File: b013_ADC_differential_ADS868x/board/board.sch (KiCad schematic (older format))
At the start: 8 parts, among them J1 002_SPI_2x5, J2 007_ADC_2x5, U1 ADS8689RUM

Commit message: added part info for silicon parts
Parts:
- U1: MPN (none) -> ADS8689RUM
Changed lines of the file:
@@
 F 2 "Package_DFN_QFN:QFN-16-1EP_4x4mm_P0.65mm_EP2.7x2.7mm" H 6425 2850 50  0001 C CNN
 F 3 "http://www.ti.com/lit/ds/symlink/ads8681.pdf" H 6475 4000 50  0001 C CNN
+F 4 "ADS8689RUM" H 6425 3750 50  0001 C CNN "MPN"
 	1    6425 3750
 	-1   0    0    -1

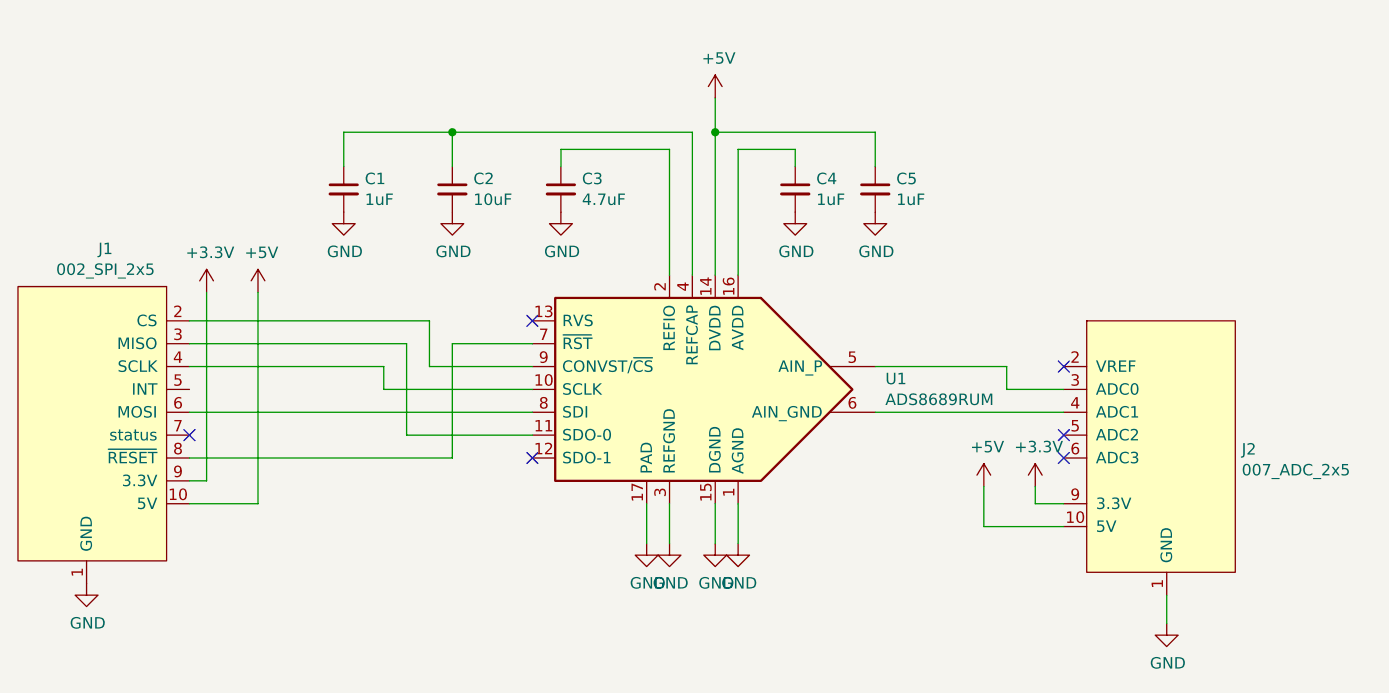
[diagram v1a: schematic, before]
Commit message: changed b013 to use 3.3v as IO voltage and fixed supply voltage bug
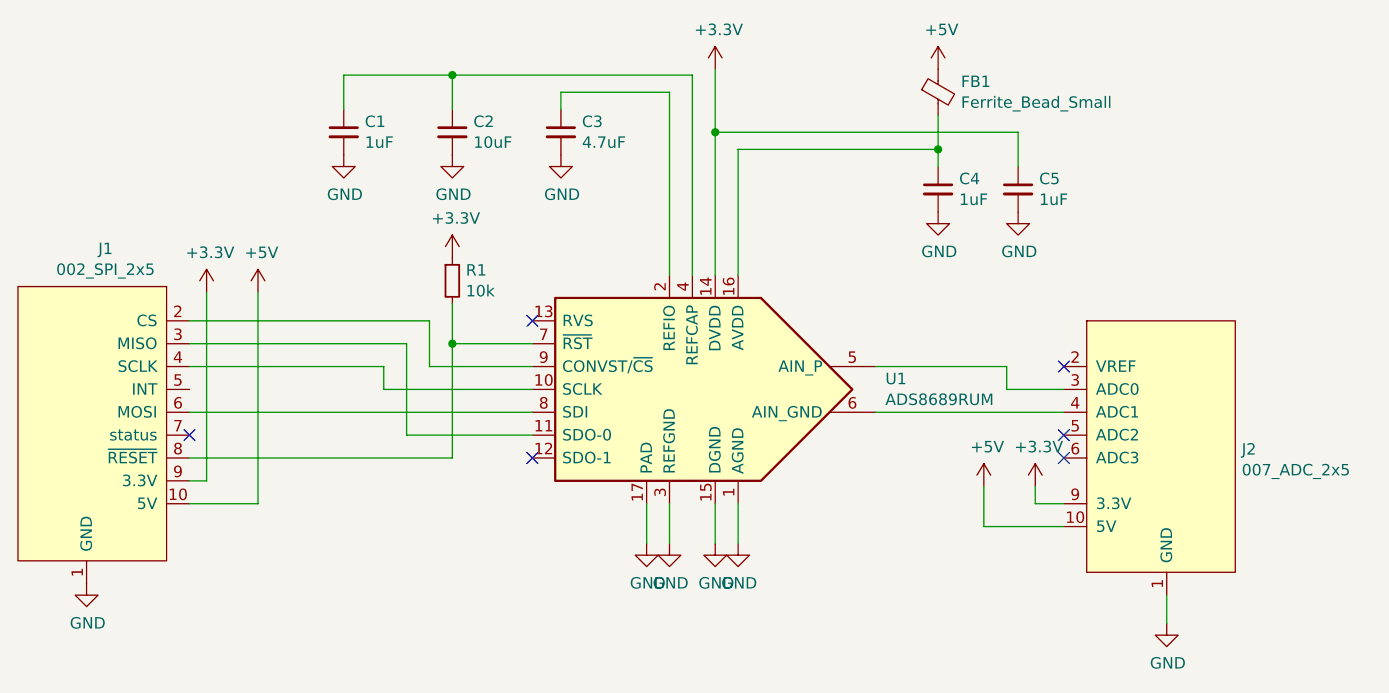
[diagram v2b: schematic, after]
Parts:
- added FB1: Ferrite_Bead_Small, Inductor_SMD:L_0603_1608Metric, symbol Device:Ferrite_Bead_Small
- added R1: 10k, Resistor_SMD:R_0603_1608Metric, symbol Device:R_Small
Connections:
- net +3V3: now also C5.1, U1.14 (DVDD), R1.1
- net +5V: now also FB1.1; no longer C5.1, U1.14 (DVDD)
- net at J1.8 (~RESET), U1.7 (~RST): now also R1.2
- net at C4.1, U1.16 (AVDD): now also FB1.2
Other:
- moved on the sheet: C1, C2, C3, C4, C5
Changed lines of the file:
@@
 L Device:C_Small C2
 U 1 1 60335A70
-P 5275 2875
-F 0 "C2" H 5367 2921 50  0000 L CNN
-F 1 "10uF" H 5367 2830 50  0000 L CNN
-F 2 "Capacitor_SMD:C_0603_1608Metric" H 5275 2875 50  0001 C CNN
-F 3 "~" H 5275 2875 50  0001 C CNN
-	1    5275 2875
+P 5275 2625
+F 0 "C2" H 5367 2671 50  0000 L CNN
+F 1 "10uF" H 5367 2580 50  0000 L CNN
+F 2 "Capacitor_SMD:C_0603_1608Metric" H 5275 2625 50  0001 C CNN
+F 3 "~" H 5275 2625 50  0001 C CNN
+	1    5275 2625
 	1    0    0    -1
 $EndComp
@@
 L Device:C_Small C1
 U 1 1 60336AFF
-P 4800 2875
-F 0 "C1" H 4892 2921 50  0000 L CNN
-F 1 "1uF" H 4892 2830 50  0000 L CNN
-F 2 "Capacitor_SMD:C_0603_1608Metric" H 4800 2875 50  0001 C CNN
-F 3 "~" H 4800 2875 50  0001 C CNN
-	1    4800 2875
-	1    0    0    -1
-$EndComp
-Wire Wire Line
-	4800 2775 4800 2625
-Wire Wire Line
-	4800 2625 5275 2625
-Wire Wire Line
-	5275 2625 5275 2775
-Wire Wire Line
-	6325 2625 6325 3250
-Connection ~ 5275 2625
-Wire Wire Line
-	5275 2625 6325 2625
+P 4800 2625
+F 0 "C1" H 4892 2671 50  0000 L CNN
+F 1 "1uF" H 4892 2580 50  0000 L CNN
+F 2 "Capacitor_SMD:C_0603_1608Metric" H 4800 2625 50  0001 C CNN
+F 3 "~" H 4800 2625 50  0001 C CNN
+	1    4800 2625
+	1    0    0    -1
+$EndComp
+Wire Wire Line
+	4800 2525 4800 2375
+Wire Wire Line
+	4800 2375 5275 2375
+Wire Wire Line
+	5275 2375 5275 2525
+Connection ~ 5275 2375
+Wire Wire Line
+	5275 2375 6325 2375
 $Comp
 L Device:C_Small C3
 U 1 1 60338ADE
-P 5750 2875
-F 0 "C3" H 5842 2921 50  0000 L CNN
-F 1 "4.7uF" H 5842 2830 50  0000 L CNN
-F 2 "Capacitor_SMD:C_0603_1608Metric" H 5750 2875 50  0001 C CNN
-F 3 "~" H 5750 2875 50  0001 C CNN
-	1    5750 2875
-	1    0    0    -1
-$EndComp
-Wire Wire Line
-	5750 2775 5750 2700
-Wire Wire Line
-	5750 2700 6225 2700
-Wire Wire Line
-	6225 2700 6225 3250
+P 5750 2625
+F 0 "C3" H 5842 2671 50  0000 L CNN
+F 1 "4.7uF" H 5842 2580 50  0000 L CNN
+F 2 "Capacitor_SMD:C_0603_1608Metric" H 5750 2625 50  0001 C CNN
+F 3 "~" H 5750 2625 50  0001 C CNN
+	1    5750 2625
+	1    0    0    -1
+$EndComp
+Wire Wire Line
+	5750 2525 5750 2450
+Wire Wire Line
+	5750 2450 6225 2450
 $Comp
 L put_on_edge:002_SPI_2x5 J1
@@
 L power:+5V #PWR0102
 U 1 1 603458CA
-P 6425 2475
-F 0 "#PWR0102" H 6425 2325 50  0001 C CNN
-F 1 "+5V" H 6440 2648 50  0000 C CNN
-F 2 "" H 6425 2475 50  0001 C CNN
-F 3 "" H 6425 2475 50  0001 C CNN
-	1    6425 2475
-	1    0    0    -1
-$EndComp
-Wire Wire Line
-	6425 2475 6425 2625
+P 7400 2350
+F 0 "#PWR0102" H 7400 2200 50  0001 C CNN
+F 1 "+5V" H 7415 2523 50  0000 C CNN
+F 2 "" H 7400 2350 50  0001 C CNN
+F 3 "" H 7400 2350 50  0001 C CNN
+	1    7400 2350
+	1    0    0    -1
+$EndComp
+Wire Wire Line
+	7400 2550 7400 2700
 $Comp
 L power:GND #PWR0103
@@
 L power:GND #PWR0107
 U 1 1 603473AA
-P 5750 2975
-F 0 "#PWR0107" H 5750 2725 50  0001 C CNN
-F 1 "GND" H 5755 2802 50  0000 C CNN
-F 2 "" H 5750 2975 50  0001 C CNN
-F 3 "" H 5750 2975 50  0001 C CNN
-	1    5750 2975
+P 5750 2725
+F 0 "#PWR0107" H 5750 2475 50  0001 C CNN
+F 1 "GND" H 5755 2552 50  0000 C CNN
+F 2 "" H 5750 2725 50  0001 C CNN
+F 3 "" H 5750 2725 50  0001 C CNN
+	1    5750 2725
 	1    0    0    -1
 $EndComp
@@
 L power:GND #PWR0108
 U 1 1 603478AD
-P 5275 2975
-F 0 "#PWR0108" H 5275 2725 50  0001 C CNN
-F 1 "GND" H 5280 2802 50  0000 C CNN
-F 2 "" H 5275 2975 50  0001 C CNN
-F 3 "" H 5275 2975 50  0001 C CNN
-	1    5275 2975
+P 5275 2725
+F 0 "#PWR0108" H 5275 2475 50  0001 C CNN
+F 1 "GND" H 5280 2552 50  0000 C CNN
+F 2 "" H 5275 2725 50  0001 C CNN
+F 3 "" H 5275 2725 50  0001 C CNN
+	1    5275 2725
 	1    0    0    -1
 $EndComp
@@
 L power:GND #PWR0109
 U 1 1 60347CB1
-P 4800 2975
-F 0 "#PWR0109" H 4800 2725 50  0001 C CNN
-F 1 "GND" H 4805 2802 50  0000 C CNN
-F 2 "" H 4800 2975 50  0001 C CNN
-F 3 "" H 4800 2975 50  0001 C CNN
-	1    4800 2975
+P 4800 2725
+F 0 "#PWR0109" H 4800 2475 50  0001 C CNN
+F 1 "GND" H 4805 2552 50  0000 C CNN
+F 2 "" H 4800 2725 50  0001 C CNN
+F 3 "" H 4800 2725 50  0001 C CNN
+	1    4800 2725
 	1    0    0    -1
 $EndComp
@@
 L Device:C_Small C4
 U 1 1 6034A12E
-P 6775 2875
-F 0 "C4" H 6867 2921 50  0000 L CNN
-F 1 "1uF" H 6867 2830 50  0000 L CNN
-F 2 "Capacitor_SMD:C_0603_1608Metric" H 6775 2875 50  0001 C CNN
-F 3 "~" H 6775 2875 50  0001 C CNN
-	1    6775 2875
+P 7400 2875
+F 0 "C4" H 7492 2921 50  0000 L CNN
+F 1 "1uF" H 7492 2830 50  0000 L CNN
+F 2 "Capacitor_SMD:C_0603_1608Metric" H 7400 2875 50  0001 C CNN
+F 3 "~" H 7400 2875 50  0001 C CNN
+	1    7400 2875
 	1    0    0    -1
 $EndComp
@@
 L power:GND #PWR0110
 U 1 1 6034A134
-P 6775 2975
-F 0 "#PWR0110" H 6775 2725 50  0001 C CNN
-F 1 "GND" H 6780 2802 50  0000 C CNN
-F 2 "" H 6775 2975 50  0001 C CNN
-F 3 "" H 6775 2975 50  0001 C CNN
-	1    6775 2975
-	1    0    0    -1
-$EndComp
-Wire Wire Line
-	6525 2700 6775 2700
-Wire Wire Line
-	6775 2700 6775 2775
+P 7400 2975
+F 0 "#PWR0110" H 7400 2725 50  0001 C CNN
+F 1 "GND" H 7405 2802 50  0000 C CNN
+F 2 "" H 7400 2975 50  0001 C CNN
+F 3 "" H 7400 2975 50  0001 C CNN
+	1    7400 2975
+	1    0    0    -1
+$EndComp
+Wire Wire Line
+	7400 2700 7400 2775
 Wire Wire Line
 	6525 2700 6525 3250
@@
 L Device:C_Small C5
 U 1 1 6035858B
-P 7125 2875
-F 0 "C5" H 7217 2921 50  0000 L CNN
-F 1 "1uF" H 7217 2830 50  0000 L CNN
-F 2 "Capacitor_SMD:C_0603_1608Metric" H 7125 2875 50  0001 C CNN
-F 3 "~" H 7125 2875 50  0001 C CNN
-	1    7125 2875
+P 7750 2875
+F 0 "C5" H 7842 2921 50  0000 L CNN
+F 1 "1uF" H 7842 2830 50  0000 L CNN
+F 2 "Capacitor_SMD:C_0603_1608Metric" H 7750 2875 50  0001 C CNN
+F 3 "~" H 7750 2875 50  0001 C CNN
+	1    7750 2875
 	1    0    0    -1
 $EndComp
@@
 L power:GND #PWR0113
 U 1 1 60358591
-P 7125 2975
-F 0 "#PWR0113" H 7125 2725 50  0001 C CNN
-F 1 "GND" H 7130 2802 50  0000 C CNN
-F 2 "" H 7125 2975 50  0001 C CNN
-F 3 "" H 7125 2975 50  0001 C CNN
-	1    7125 2975
-	1    0    0    -1
-$EndComp
-Wire Wire Line
-	7125 2775 7125 2625
-Wire Wire Line
-	7125 2625 6425 2625
-Connection ~ 6425 2625
+P 7750 2975
+F 0 "#PWR0113" H 7750 2725 50  0001 C CNN
+F 1 "GND" H 7755 2802 50  0000 C CNN
+F 2 "" H 7750 2975 50  0001 C CNN
+F 3 "" H 7750 2975 50  0001 C CNN
+	1    7750 2975
+	1    0    0    -1
+$EndComp
+Wire Wire Line
+	7750 2775 7750 2625
 Wire Wire Line
 	6425 2625 6425 3250
@@
 Wire Wire Line
 	7825 4250 7950 4250
+Connection ~ 7400 2700
+$Comp
+L Device:Ferrite_Bead_Small FB1
+U 1 1 607A183C
+P 7400 2450
+F 0 "FB1" H 7500 2496 50  0000 L CNN
+F 1 "Ferrite_Bead_Small" H 7500 2405 50  0000 L CNN
+F 2 "Inductor_SMD:L_0603_1608Metric" V 7330 2450 50  0001 C CNN
+F 3 "~" H 7400 2450 50  0001 C CNN
+	1    7400 2450
+	1    0    0    -1
+$EndComp
+Wire Wire Line
+	6525 2700 7400 2700
+Wire Wire Line
+	6425 2625 7750 2625
+$Comp
+L power:+3.3V #PWR0117
+U 1 1 607A9415
+P 6425 2350
+F 0 "#PWR0117" H 6425 2200 50  0001 C CNN
+F 1 "+3.3V" H 6440 2523 50  0000 C CNN
+F 2 "" H 6425 2350 50  0001 C CNN
+F 3 "" H 6425 2350 50  0001 C CNN
+	1    6425 2350
+	1    0    0    -1
+$EndComp
+Wire Wire Line
+	6425 2350 6425 2625
+Connection ~ 6425 2625
+Wire Wire Line
+	6225 2450 6225 3250
+Wire Wire Line
+	6325 2375 6325 3250
+$Comp
+L Device:R_Small R1
+U 1 1 607B017C
+P 5275 3275
+F 0 "R1" H 5334 3321 50  0000 L CNN
+F 1 "10k" H 5334 3230 50  0000 L CNN
+F 2 "Resistor_SMD:R_0603_1608Metric" H 5275 3275 50  0001 C CNN
+F 3 "~" H 5275 3275 50  0001 C CNN
+	1    5275 3275
+	1    0    0    -1
+$EndComp
+Wire Wire Line
+	5275 3550 5275 3375
+Connection ~ 5275 3550
+$Comp
+L power:+3.3V #PWR0118
+U 1 1 607B1592
+P 5275 3175
+F 0 "#PWR0118" H 5275 3025 50  0001 C CNN
+F 1 "+3.3V" H 5290 3348 50  0000 C CNN
+F 2 "" H 5275 3175 50  0001 C CNN
+F 3 "" H 5275 3175 50  0001 C CNN
+	1    5275 3175
+	1    0    0    -1
+$EndComp
 $EndSCHEMATC

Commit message: fixed connectors and power bug
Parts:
- J1: symbol put_on_edge:002_SPI_2x5 -> put_on_edge:002_SPI
- J2: symbol put_on_edge:007_ADC_2x5 -> put_on_edge:007_ADC
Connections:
- net at J1.2 (MOSI): now also U1.8 (SDI); no longer U1.9 (CONVST/~CS)
- net at J1.6 (CS): now also U1.9 (CONVST/~CS); no longer U1.8 (SDI)
- no-connect marks 6 -> 7
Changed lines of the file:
@@
 	5750 2450 6225 2450
 $Comp
-L put_on_edge:002_SPI_2x5 J1
+L put_on_edge:002_SPI J1
 U 1 1 6033E642
 P 3675 3800
@@
 $EndComp
 Wire Wire Line
-	4125 3450 5175 3450
-Wire Wire Line
-	5175 3450 5175 3650
-Wire Wire Line
-	4125 3550 5075 3550
-Wire Wire Line
-	5075 3950 5625 3950
-Wire Wire Line
-	5075 3550 5075 3950
-Wire Wire Line
-	5625 3850 4125 3850
-Wire Wire Line
-	5625 3650 5175 3650
-Wire Wire Line
-	4975 3750 4975 3650
-Wire Wire Line
-	4975 3650 4125 3650
-Wire Wire Line
-	4975 3750 5625 3750
-Wire Wire Line
 	5625 3550 5275 3550
 Wire Wire Line
 	5275 3550 5275 4050
-Wire Wire Line
-	5275 4050 4125 4050
 NoConn ~ 5625 4050
 NoConn ~ 5625 3450
@@
 	6425 2625 6425 3250
 $Comp
-L put_on_edge:007_ADC_2x5 J2
+L put_on_edge:007_ADC J2
 U 1 1 6034A82D
 P 8400 3950
@@
 	1    0    0    -1
 $EndComp
+Wire Wire Line
+	4125 4050 5275 4050
+Wire Wire Line
+	4300 3950 4300 3550
+Wire Wire Line
+	4300 3550 4125 3550
+Wire Wire Line
+	4300 3950 5625 3950
+Wire Wire Line
+	5625 3850 5175 3850
+Wire Wire Line
+	5175 3850 5175 3450
+Wire Wire Line
+	5175 3450 4125 3450
+Wire Wire Line
+	4650 3750 4650 3650
+Wire Wire Line
+	4650 3650 4125 3650
+Wire Wire Line
+	4650 3750 5625 3750
+NoConn ~ 4125 3750
+Wire Wire Line
+	4125 3850 4900 3850
+Wire Wire Line
+	4900 3850 4900 3650
+Wire Wire Line
+	4900 3650 5625 3650
 $EndSCHEMATC
